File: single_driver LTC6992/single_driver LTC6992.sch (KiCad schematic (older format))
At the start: 33 parts, among them J2 Screw_Terminal_01x02, J3 Conn_01x08_Male, U2 LM7805_TO220, U3 DRV10970

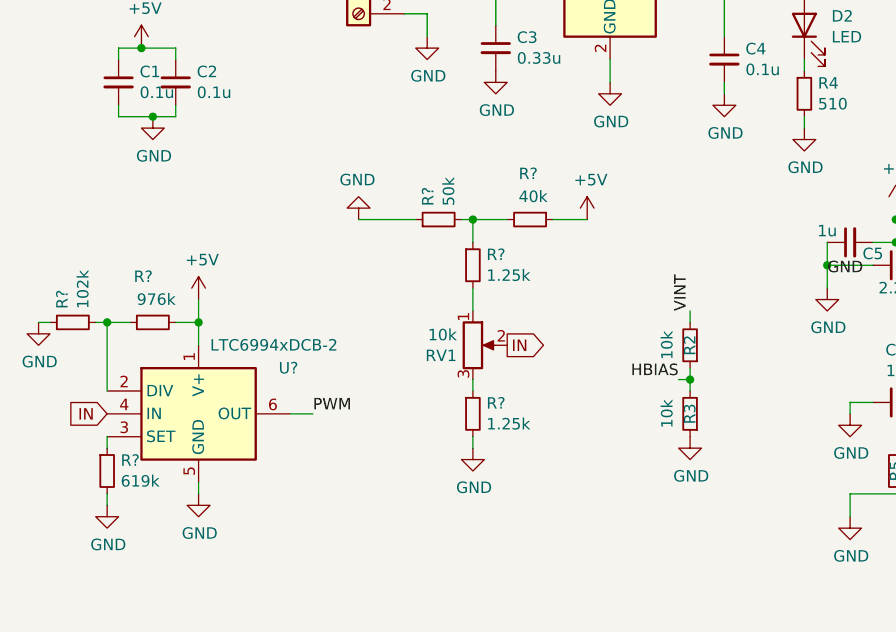
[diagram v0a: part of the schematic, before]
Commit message: Added header for lock and tach
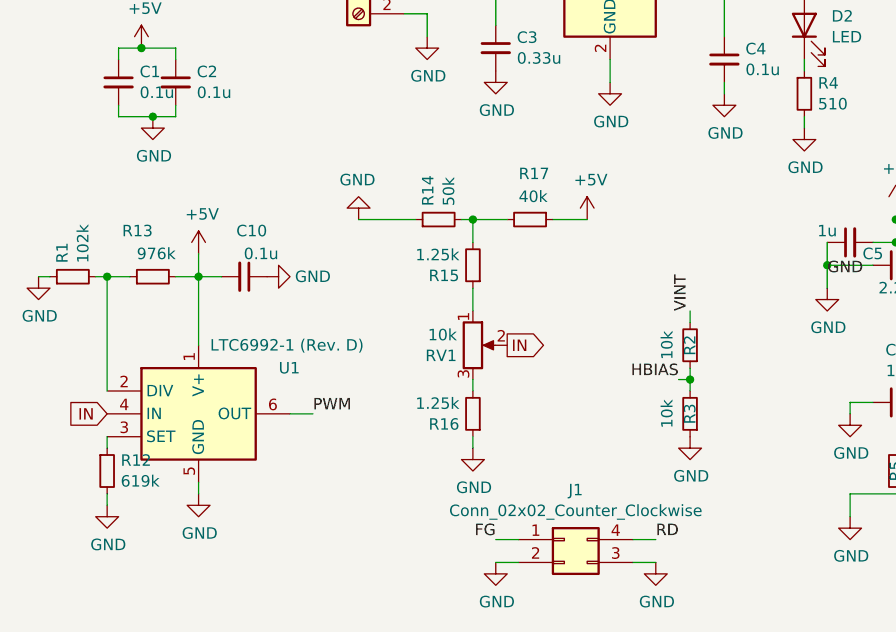
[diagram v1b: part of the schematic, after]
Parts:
- removed R? (x2): 1.25k, Resistor_SMD:R_0603_1608Metric, symbol Device:R_Small
- added C10: 0.1u, Capacitor_SMD:C_0603_1608Metric, symbol Device:C_Small
- added J1: Conn_02x02_Counter_Clockwise, Connector_PinHeader_2.54mm:PinHeader_2x02_P2.54mm_Vertical, symbol Connector_Generic:Conn_02x02_Counter_Clockwise
- added R15, R16: 1.25k, Resistor_SMD:R_0603_1608Metric, symbol Device:R_Small
- U1: renamed from U?; value LTC6994xDCB-2 -> LTC6992-1 (Rev. D)
- gave numbers to parts that had none: 5
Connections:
- net +5V: now also C10.2
- net FG: now also J1.1 (Pin_1)
- net GND: now also C10.1, J1.2 (Pin_2), J1.3 (Pin_3), R16.1
- net RD: now also J1.4 (Pin_4)
- net at RV1.1: now also R15.1
- net at RV1.3: now also R16.2
- net at R14.2, R17.2: now also R15.2
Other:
- moved on the sheet: R1, R13

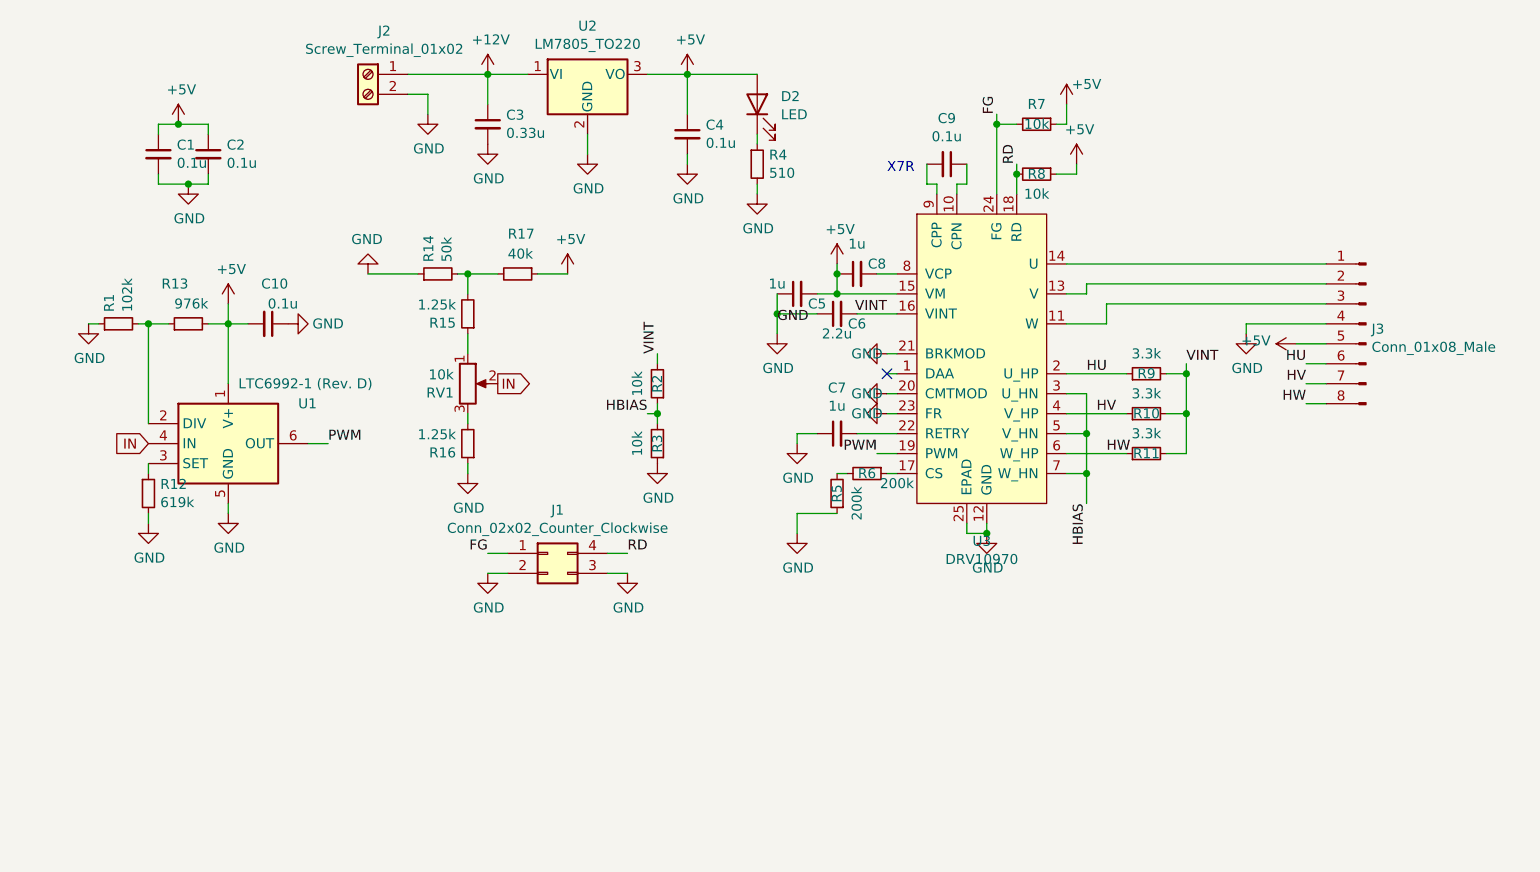
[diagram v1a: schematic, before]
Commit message: Added DIP switch
DIP switch will control various aspects of the control algorithm
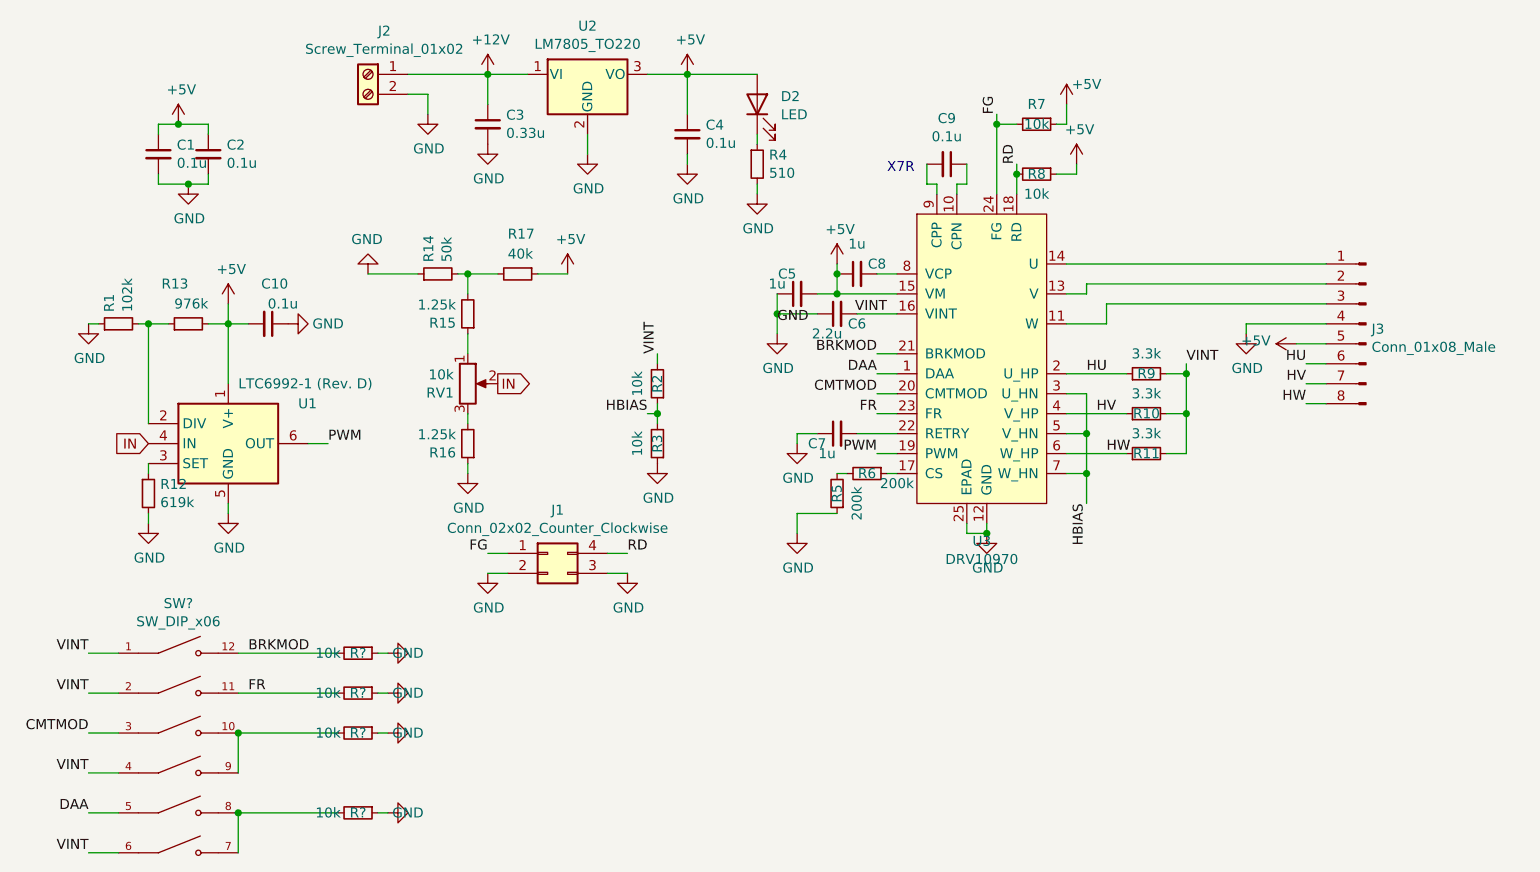
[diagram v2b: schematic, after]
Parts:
- added R? (x4): 10k, Resistor_SMD:R_0603_1608Metric, symbol Device:R_Small
- added SW?: SW_DIP_x06, HS2_parts:DIP762W56P254L1772H585Q12, symbol 1825057-5:1825057-5
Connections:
- net GND: now also R?.1, R?.1, R?.1, R?.1; no longer U3.20 (CMTMOD), U3.21 (BRKMOD), U3.23 (FR)
- net VINT: now also SW?.1, SW?.2, SW?.4, SW?.6
- net DAA: now reaches U3.1 (DAA)
- net DAA: now also SW?.5
- new net: R?.2, SW?.10, SW?.9
- new net: R?.2, SW?.7, SW?.8
- new net BRKMOD: R?.2, SW?.12, U3.21 (BRKMOD)
- new net CMTMOD: SW?.3, U3.20 (CMTMOD)
- new net FR: R?.2, SW?.11, U3.23 (FR)
- no-connect marks 1 -> 0
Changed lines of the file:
@@
 	0    1    1    0
-$EndComp
-$Comp
-L HS2_Parts:DRV10970 U3
-U 1 1 5F9EAE81
-P 7300 3400
-F 0 "U3" H 7375 2411 50  0000 C CNN
-F 1 "DRV10970" H 7375 2320 50  0000 C CNN
-F 2 "Package_SO:HTSSOP-24-1EP_4.4x7.8mm_P0.65mm_EP3.4x7.8mm_Mask2.4x4.68mm_ThermalVias" H 7300 3400 50  0001 C CNN
-F 3 "https://www.ti.com/lit/ds/symlink/drv10970.pdf?HQS=TI-null-null-digikeymode-df-pf-null-wwe&ts=1604208046281" H 7300 3400 50  0001 C CNN
-	1    7300 3400
-	1    0    0    -1
 $EndComp
 Wire Wire Line
@@
 P 6650 3250
 F 0 "C6" V 6600 3150 50  0000 C CNN
-F 1 "2.2u" V 6550 3250 50  0000 C CNN
+F 1 "2.2u" V 6550 3300 50  0000 C CNN
 F 2 "Capacitor_SMD:C_0603_1608Metric" H 6650 3250 50  0001 C CNN
 F 3 "~" H 6650 3250 50  0001 C CNN
@@
 U 1 1 5F9F51E6
 P 6450 3150
-F 0 "C5" V 6400 3050 50  0000 C CNN
+F 0 "C5" V 6550 3200 50  0000 C CNN
 F 1 "1u" V 6500 3250 50  0000 C CNN
 F 2 "Capacitor_SMD:C_0603_1608Metric" H 6450 3150 50  0001 C CNN
@@
 	1    0    0    -1
 $EndComp
-$Comp
-L Device:C_Small C7
-U 1 1 5F9F8DC5
-P 6650 3850
-F 0 "C7" V 6421 3850 50  0000 C CNN
-F 1 "1u" V 6512 3850 50  0000 C CNN
-F 2 "Capacitor_SMD:C_0603_1608Metric" H 6650 3850 50  0001 C CNN
-F 3 "~" H 6650 3850 50  0001 C CNN
-	1    6650 3850
-	0    -1   1    0
-$EndComp
-Wire Wire Line
-	6950 3850 6750 3850
 Wire Wire Line
 	6550 3850 6450 3850
@@
 Wire Wire Line
 	6450 4250 6450 4350
-Wire Wire Line
-	6950 3450 6900 3450
-Wire Wire Line
-	6950 3650 6900 3650
-Wire Wire Line
-	6950 3750 6900 3750
 $Comp
 L power:GND #PWR0109
@@
 	4800 3050 4750 3050
 $Comp
-L power:GND #PWR0126
-U 1 1 5FDE9AF2
-P 6900 3750
-F 0 "#PWR0126" H 6900 3500 50  0001 C CNN
-F 1 "GND" V 6900 3650 50  0000 C CNN
-F 2 "" H 6900 3750 50  0001 C CNN
-F 3 "" H 6900 3750 50  0001 C CNN
-	1    6900 3750
-	0    1    1    0
-$EndComp
-$Comp
-L power:GND #PWR0127
-U 1 1 5FDEABE6
-P 6900 3650
-F 0 "#PWR0127" H 6900 3400 50  0001 C CNN
-F 1 "GND" V 6900 3550 50  0000 C CNN
-F 2 "" H 6900 3650 50  0001 C CNN
-F 3 "" H 6900 3650 50  0001 C CNN
-	1    6900 3650
-	0    1    1    0
-$EndComp
-Wire Wire Line
-	6950 3550 6900 3550
-NoConn ~ 6900 3550
-$Comp
-L power:GND #PWR0128
-U 1 1 5FDFE31C
-P 6900 3450
-F 0 "#PWR0128" H 6900 3200 50  0001 C CNN
-F 1 "GND" V 6900 3350 50  0000 C CNN
-F 2 "" H 6900 3450 50  0001 C CNN
-F 3 "" H 6900 3450 50  0001 C CNN
-	1    6900 3450
-	0    1    1    0
-$EndComp
-$Comp
 L Device:C_Small C10
 U 1 1 5FE4181E
@@
 	-1   0    0    1
 $EndComp
+Text Label 2900 4950 2    50   ~ 0
+VINT
+Text Label 2900 5150 2    50   ~ 0
+VINT
+Text Label 2900 5550 2    50   ~ 0
+VINT
+$Comp
+L Device:R_Small R?
+U 1 1 5FD8CC05
+P 4250 5350
+F 0 "R?" V 4250 5350 50  0000 C CNN
+F 1 "10k" V 4250 5200 50  0000 C CNN
+F 2 "Resistor_SMD:R_0603_1608Metric" H 4250 5350 50  0001 C CNN
+F 3 "~" H 4250 5350 50  0001 C CNN
+	1    4250 5350
+	0    1    1    0
+$EndComp
+$Comp
+L 1825057-5:1825057-5 SW?
+U 1 1 5FD8A0DD
+P 3350 5450
+F 0 "SW?" H 3350 6199 50  0000 C CNN
+F 1 "SW_DIP_x06" H 3350 6108 50  0000 C CNN
+F 2 "HS2_parts:DIP762W56P254L1772H585Q12" H 3350 5450 50  0001 C CNN
+F 3 "~" H 3350 5450 50  0001 C CNN
+	1    3350 5450
+	1    0    0    -1
+$EndComp
+$Comp
+L HS2_Parts:DRV10970 U3
+U 1 1 5F9EAE81
+P 7300 3400
+F 0 "U3" H 7375 2411 50  0000 C CNN
+F 1 "DRV10970" H 7375 2320 50  0000 C CNN
+F 2 "Package_SO:HTSSOP-24-1EP_4.4x7.8mm_P0.65mm_EP3.4x7.8mm_Mask2.4x4.68mm_ThermalVias" H 7300 3400 50  0001 C CNN
+F 3 "https://www.ti.com/lit/ds/symlink/drv10970.pdf?HQS=TI-null-null-digikeymode-df-pf-null-wwe&ts=1604208046281" H 7300 3400 50  0001 C CNN
+	1    7300 3400
+	1    0    0    -1
+$EndComp
+Text Label 6850 3450 2    50   ~ 0
+BRKMOD
+Text Label 6850 3650 2    50   ~ 0
+CMTMOD
+Text Label 6850 3750 2    50   ~ 0
+FR
+Text Label 3700 4950 0    50   ~ 0
+BRKMOD
+Text Label 3700 5150 0    50   ~ 0
+FR
+Text Label 2900 5350 2    50   ~ 0
+CMTMOD
+Text Label 2900 5950 2    50   ~ 0
+VINT
+Wire Wire Line
+	6950 3850 6750 3850
+Wire Wire Line
+	4400 4950 4350 4950
+Wire Wire Line
+	4400 5150 4350 5150
+$Comp
+L Device:R_Small R?
+U 1 1 5FD91E5A
+P 4250 4950
+F 0 "R?" V 4250 4950 50  0000 C CNN
+F 1 "10k" V 4250 4800 50  0000 C CNN
+F 2 "Resistor_SMD:R_0603_1608Metric" H 4250 4950 50  0001 C CNN
+F 3 "~" H 4250 4950 50  0001 C CNN
+	1    4250 4950
+	0    1    1    0
+$EndComp
+$Comp
+L Device:R_Small R?
+U 1 1 5FD9157F
+P 4250 5150
+F 0 "R?" V 4250 5150 50  0000 C CNN
+F 1 "10k" V 4250 5000 50  0000 C CNN
+F 2 "Resistor_SMD:R_0603_1608Metric" H 4250 5150 50  0001 C CNN
+F 3 "~" H 4250 5150 50  0001 C CNN
+	1    4250 5150
+	0    1    1    0
+$EndComp
+$Comp
+L power:GND #PWR0128
+U 1 1 5FDFE31C
+P 4400 5350
+F 0 "#PWR0128" H 4400 5100 50  0001 C CNN
+F 1 "GND" V 4400 5250 50  0000 C CNN
+F 2 "" H 4400 5350 50  0001 C CNN
+F 3 "" H 4400 5350 50  0001 C CNN
+	1    4400 5350
+	0    -1   -1   0
+$EndComp
+$Comp
+L power:GND #PWR0127
+U 1 1 5FDEABE6
+P 4400 5150
+F 0 "#PWR0127" H 4400 4900 50  0001 C CNN
+F 1 "GND" V 4400 5050 50  0000 C CNN
+F 2 "" H 4400 5150 50  0001 C CNN
+F 3 "" H 4400 5150 50  0001 C CNN
+	1    4400 5150
+	0    -1   -1   0
+$EndComp
+$Comp
+L power:GND #PWR0126
+U 1 1 5FDE9AF2
+P 4400 4950
+F 0 "#PWR0126" H 4400 4700 50  0001 C CNN
+F 1 "GND" V 4400 4850 50  0000 C CNN
+F 2 "" H 4400 4950 50  0001 C CNN
+F 3 "" H 4400 4950 50  0001 C CNN
+	1    4400 4950
+	0    -1   -1   0
+$EndComp
+$Comp
+L Device:C_Small C7
+U 1 1 5F9F8DC5
+P 6650 3850
+F 0 "C7" V 6700 3950 50  0000 C CNN
+F 1 "1u" V 6750 3900 50  0000 C CNN
+F 2 "Capacitor_SMD:C_0603_1608Metric" H 6650 3850 50  0001 C CNN
+F 3 "~" H 6650 3850 50  0001 C CNN
+	1    6650 3850
+	0    -1   1    0
+$EndComp
+Text Label 6850 3550 2    50   ~ 0
+DAA
+Wire Wire Line
+	6850 3450 6950 3450
+Wire Wire Line
+	6850 3550 6950 3550
+Wire Wire Line
+	6850 3650 6950 3650
+Wire Wire Line
+	6850 3750 6950 3750
+Text Label 2900 5750 2    50   ~ 0
+DAA
+Wire Wire Line
+	3650 4950 4150 4950
+Wire Wire Line
+	3650 5150 4150 5150
+Wire Wire Line
+	4350 5350 4400 5350
+$Comp
+L Device:R_Small R?
+U 1 1 5FE57D67
+P 4250 5750
+F 0 "R?" V 4250 5750 50  0000 C CNN
+F 1 "10k" V 4250 5600 50  0000 C CNN
+F 2 "Resistor_SMD:R_0603_1608Metric" H 4250 5750 50  0001 C CNN
+F 3 "~" H 4250 5750 50  0001 C CNN
+	1    4250 5750
+	0    1    1    0
+$EndComp
+$Comp
+L power:GND #PWR?
+U 1 1 5FE58061
+P 4400 5750
+F 0 "#PWR?" H 4400 5500 50  0001 C CNN
+F 1 "GND" V 4400 5650 50  0000 C CNN
+F 2 "" H 4400 5750 50  0001 C CNN
+F 3 "" H 4400 5750 50  0001 C CNN
+	1    4400 5750
+	0    -1   -1   0
+$EndComp
+Wire Wire Line
+	3650 5750 4150 5750
+Wire Wire Line
+	4350 5750 4400 5750
+Wire Wire Line
+	3650 5550 3650 5350
+Connection ~ 3650 5350
+Wire Wire Line
+	3650 5950 3650 5750
+Wire Wire Line
+	3650 5350 4150 5350
+Connection ~ 3650 5750
+Wire Wire Line
+	3050 5950 2900 5950
+Wire Wire Line
+	3050 5750 2900 5750
+Wire Wire Line
+	3050 5550 2900 5550
+Wire Wire Line
+	3050 5350 2900 5350
+Wire Wire Line
+	3050 5150 2900 5150
+Wire Wire Line
+	3050 4950 2900 4950
 $EndSCHEMATC

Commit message: Slight changes
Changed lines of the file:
@@
 	1    0    0    -1
 $EndComp
-Text GLabel 4950 3600 2    50   Output ~ 0
-IN
-Text GLabel 3200 3900 0    50   Input ~ 0
-IN
 Wire Wire Line
 	3600 3300 3500 3300
@@
 Wire Wire Line
 	3050 4950 2900 4950
+Text Label 5000 3600 0    50   ~ 0
+IN
+Text Label 3150 3900 2    50   ~ 0
+IN
+Wire Wire Line
+	5000 3600 4950 3600
+Wire Wire Line
+	3200 3900 3150 3900
 $EndSCHEMATC

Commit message: Started PCB
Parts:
- gave numbers to parts that had none: 5
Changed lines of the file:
@@
 VINT
 $Comp
-L Device:R_Small R?
+L Device:R_Small R20
 U 1 1 5FD8CC05
 P 4250 5350
-F 0 "R?" V 4250 5350 50  0000 C CNN
+F 0 "R20" V 4250 5350 50  0000 C CNN
 F 1 "10k" V 4250 5200 50  0000 C CNN
 F 2 "Resistor_SMD:R_0603_1608Metric" H 4250 5350 50  0001 C CNN
@@
 $EndComp
 $Comp
-L 1825057-5:1825057-5 SW?
+L 1825057-5:1825057-5 SW1
 U 1 1 5FD8A0DD
 P 3350 5450
-F 0 "SW?" H 3350 6199 50  0000 C CNN
+F 0 "SW1" H 3350 6199 50  0000 C CNN
 F 1 "SW_DIP_x06" H 3350 6108 50  0000 C CNN
 F 2 "HS2_parts:DIP762W56P254L1772H585Q12" H 3350 5450 50  0001 C CNN
@@
 	4400 5150 4350 5150
 $Comp
-L Device:R_Small R?
+L Device:R_Small R18
 U 1 1 5FD91E5A
 P 4250 4950
-F 0 "R?" V 4250 4950 50  0000 C CNN
+F 0 "R18" V 4250 4950 50  0000 C CNN
 F 1 "10k" V 4250 4800 50  0000 C CNN
 F 2 "Resistor_SMD:R_0603_1608Metric" H 4250 4950 50  0001 C CNN
@@
 $EndComp
 $Comp
-L Device:R_Small R?
+L Device:R_Small R19
 U 1 1 5FD9157F
 P 4250 5150
-F 0 "R?" V 4250 5150 50  0000 C CNN
+F 0 "R19" V 4250 5150 50  0000 C CNN
 F 1 "10k" V 4250 5000 50  0000 C CNN
 F 2 "Resistor_SMD:R_0603_1608Metric" H 4250 5150 50  0001 C CNN
@@
 	4350 5350 4400 5350
 $Comp
-L Device:R_Small R?
+L Device:R_Small R21
 U 1 1 5FE57D67
 P 4250 5750
-F 0 "R?" V 4250 5750 50  0000 C CNN
+F 0 "R21" V 4250 5750 50  0000 C CNN
 F 1 "10k" V 4250 5600 50  0000 C CNN
 F 2 "Resistor_SMD:R_0603_1608Metric" H 4250 5750 50  0001 C CNN
@@
 $EndComp
 $Comp
-L power:GND #PWR?
+L power:GND #PWR0133
 U 1 1 5FE58061
 P 4400 5750
-F 0 "#PWR?" H 4400 5500 50  0001 C CNN
+F 0 "#PWR0133" H 4400 5500 50  0001 C CNN
 F 1 "GND" V 4400 5650 50  0000 C CNN
 F 2 "" H 4400 5750 50  0001 C CNN

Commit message: Changed current sensing resistor
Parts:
- removed R5: 200k, Resistor_SMD:R_0603_1608Metric, symbol Device:R_Small
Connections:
- net GND: now also R6.2
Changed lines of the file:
@@
 Text Notes 6900 2550 0    50   ~ 0
 X7R
-$Comp
-L Device:R_Small R5
-U 1 1 5FA742C3
-P 6650 4150
-F 0 "R5" V 6650 4150 50  0000 C CNN
-F 1 "200k" V 6550 4200 50  0000 C CNN
-F 2 "Resistor_SMD:R_0603_1608Metric" H 6650 4150 50  0001 C CNN
-F 3 "~" H 6650 4150 50  0001 C CNN
-	1    6650 4150
-	-1   0    0    1
-$EndComp
 Wire Wire Line
 	6650 4050 6700 4050
@@
 Wire Wire Line
 	3200 3900 3150 3900
+Wire Wire Line
+	6650 4050 6650 4250
 $EndSCHEMATC

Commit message: Basically finished pcb
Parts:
- R18, R19, R20, R21: value 10k -> 100k
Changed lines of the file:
@@
 P 4250 5350
 F 0 "R20" V 4250 5350 50  0000 C CNN
-F 1 "10k" V 4250 5200 50  0000 C CNN
+F 1 "100k" V 4200 5150 50  0000 C CNN
 F 2 "Resistor_SMD:R_0603_1608Metric" H 4250 5350 50  0001 C CNN
 F 3 "~" H 4250 5350 50  0001 C CNN
@@
 P 4250 4950
 F 0 "R18" V 4250 4950 50  0000 C CNN
-F 1 "10k" V 4250 4800 50  0000 C CNN
+F 1 "100k" V 4150 4750 50  0000 C CNN
 F 2 "Resistor_SMD:R_0603_1608Metric" H 4250 4950 50  0001 C CNN
 F 3 "~" H 4250 4950 50  0001 C CNN
@@
 P 4250 5150
 F 0 "R19" V 4250 5150 50  0000 C CNN
-F 1 "10k" V 4250 5000 50  0000 C CNN
+F 1 "100k" V 4200 4950 50  0000 C CNN
 F 2 "Resistor_SMD:R_0603_1608Metric" H 4250 5150 50  0001 C CNN
 F 3 "~" H 4250 5150 50  0001 C CNN
@@
 P 4250 5750
 F 0 "R21" V 4250 5750 50  0000 C CNN
-F 1 "10k" V 4250 5600 50  0000 C CNN
+F 1 "100k" V 4150 5550 50  0000 C CNN
 F 2 "Resistor_SMD:R_0603_1608Metric" H 4250 5750 50  0001 C CNN
 F 3 "~" H 4250 5750 50  0001 C CNN
